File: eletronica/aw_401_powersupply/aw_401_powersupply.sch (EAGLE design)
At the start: 13 parts

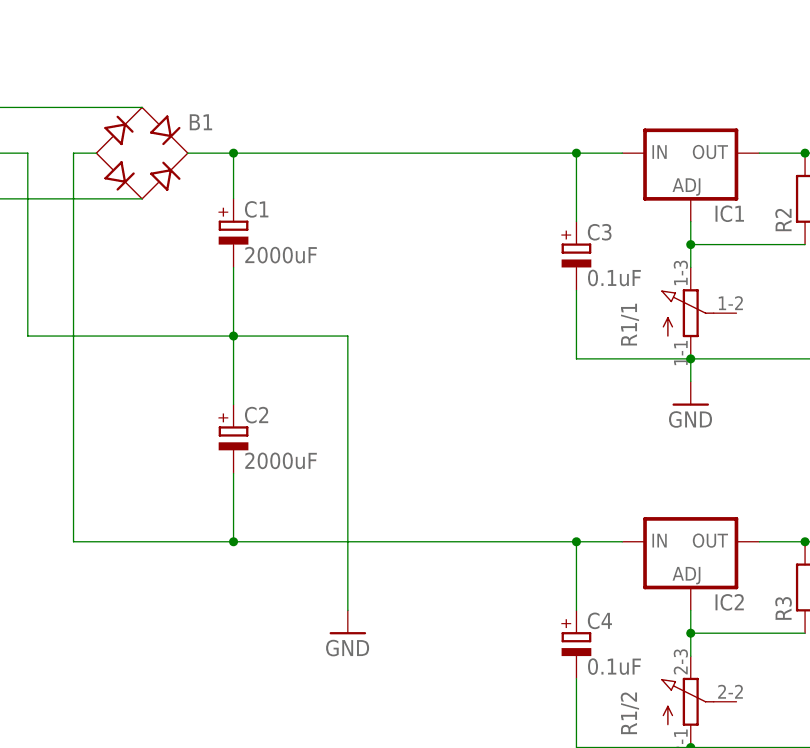
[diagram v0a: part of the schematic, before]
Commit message: 
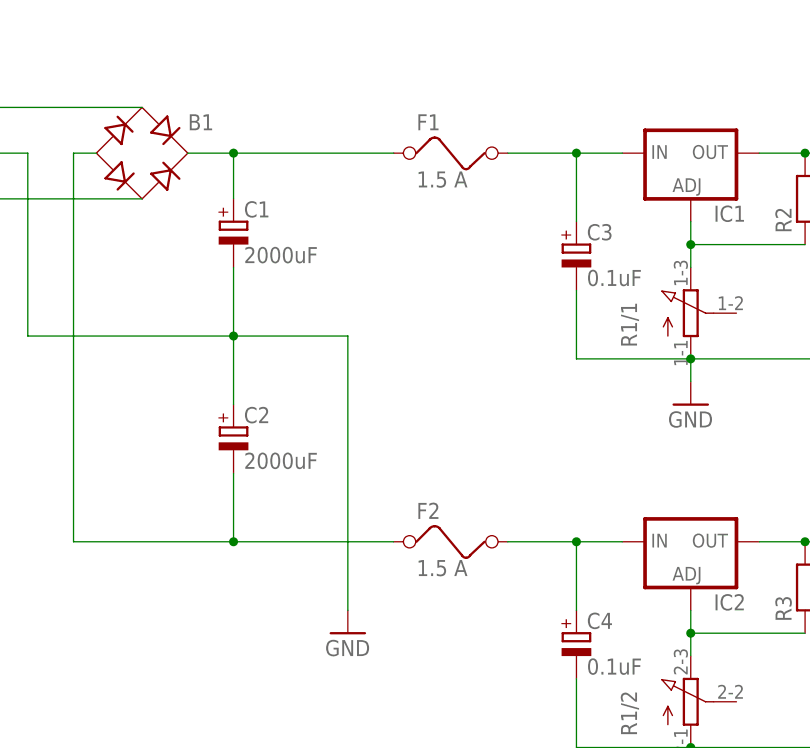
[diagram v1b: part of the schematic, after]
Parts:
- added F1, F2: 1.5 A, special:FUSE
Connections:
- new net N$10: C3.+, F1.2, IC1.IN
- new net N$9: C4.+, F2.2, IC2.IN
- net N$3: now also F1.1; no longer C3.+, IC1.IN
- net N$5: now also F2.1; no longer C4.+, IC2.IN
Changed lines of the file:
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@@
 <part name="C5" library="resistor" deviceset="CPOL-EU" device="E2.5-6" value="1uF"/>
 <part name="C6" library="resistor" deviceset="CPOL-EU" device="E2.5-6" value="1uF"/>
+<part name="F1" library="special" deviceset="FUSE" device="" value="1.5 A"/>
+<part name="F2" library="special" deviceset="FUSE" device="" value="1.5 A"/>
 </parts>
 <sheets>
@@
 <instance part="C5" gate="G$1" x="124.46" y="63.5"/>
 <instance part="C6" gate="G$1" x="124.46" y="20.32"/>
+<instance part="F1" gate="G$1" x="76.2" y="73.66"/>
+<instance part="F2" gate="G$1" x="76.2" y="30.48"/>
 </instances>
 <busses>
@@
 <wire x1="45.72" y1="73.66" x2="50.8" y2="73.66" width="0.1524" layer="91"/>
 <wire x1="50.8" y1="73.66" x2="50.8" y2="68.58" width="0.1524" layer="91"/>
-<wire x1="50.8" y1="73.66" x2="88.9" y2="73.66" width="0.1524" layer="91"/>
+<wire x1="50.8" y1="73.66" x2="68.58" y2="73.66" width="0.1524" layer="91"/>
 <junction x="50.8" y="73.66"/>
-<pinref part="IC1" gate="1" pin="IN"/>
-<pinref part="C3" gate="G$1" pin="+"/>
-<wire x1="88.9" y1="73.66" x2="93.98" y2="73.66" width="0.1524" layer="91"/>
-<wire x1="88.9" y1="73.66" x2="88.9" y2="66.04" width="0.1524" layer="91"/>
-<junction x="88.9" y="73.66"/>
+<pinref part="F1" gate="G$1" pin="1"/>
 </segment>
 </net>
@@
 <wire x1="33.02" y1="30.48" x2="50.8" y2="30.48" width="0.1524" layer="91"/>
 <wire x1="50.8" y1="30.48" x2="50.8" y2="38.1" width="0.1524" layer="91"/>
-<wire x1="50.8" y1="30.48" x2="88.9" y2="30.48" width="0.1524" layer="91"/>
+<wire x1="50.8" y1="30.48" x2="68.58" y2="30.48" width="0.1524" layer="91"/>
 <junction x="50.8" y="30.48"/>
-<pinref part="IC2" gate="1" pin="IN"/>
-<pinref part="C4" gate="G$1" pin="+"/>
-<wire x1="88.9" y1="30.48" x2="93.98" y2="30.48" width="0.1524" layer="91"/>
-<wire x1="88.9" y1="30.48" x2="88.9" y2="22.86" width="0.1524" layer="91"/>
-<junction x="88.9" y="30.48"/>
+<pinref part="F2" gate="G$1" pin="1"/>
 </segment>
 </net>
@@
 </segment>
 </net>
+<net name="N$9" class="0">
+<segment>
+<pinref part="C4" gate="G$1" pin="+"/>
+<pinref part="IC2" gate="1" pin="IN"/>
+<wire x1="88.9" y1="30.48" x2="93.98" y2="30.48" width="0.1524" layer="91"/>
+<wire x1="88.9" y1="30.48" x2="88.9" y2="22.86" width="0.1524" layer="91"/>
+<junction x="88.9" y="30.48"/>
+<wire x1="81.28" y1="30.48" x2="88.9" y2="30.48" width="0.1524" layer="91"/>
+<pinref part="F2" gate="G$1" pin="2"/>
+</segment>
+</net>
+<net name="N$10" class="0">
+<segment>
+<pinref part="C3" gate="G$1" pin="+"/>
+<pinref part="IC1" gate="1" pin="IN"/>
+<wire x1="88.9" y1="73.66" x2="93.98" y2="73.66" width="0.1524" layer="91"/>
+<wire x1="88.9" y1="73.66" x2="88.9" y2="66.04" width="0.1524" layer="91"/>
+<junction x="88.9" y="73.66"/>
+<wire x1="81.28" y1="73.66" x2="88.9" y2="73.66" width="0.1524" layer="91"/>
+<pinref part="F1" gate="G$1" pin="2"/>
+</segment>
+</net>

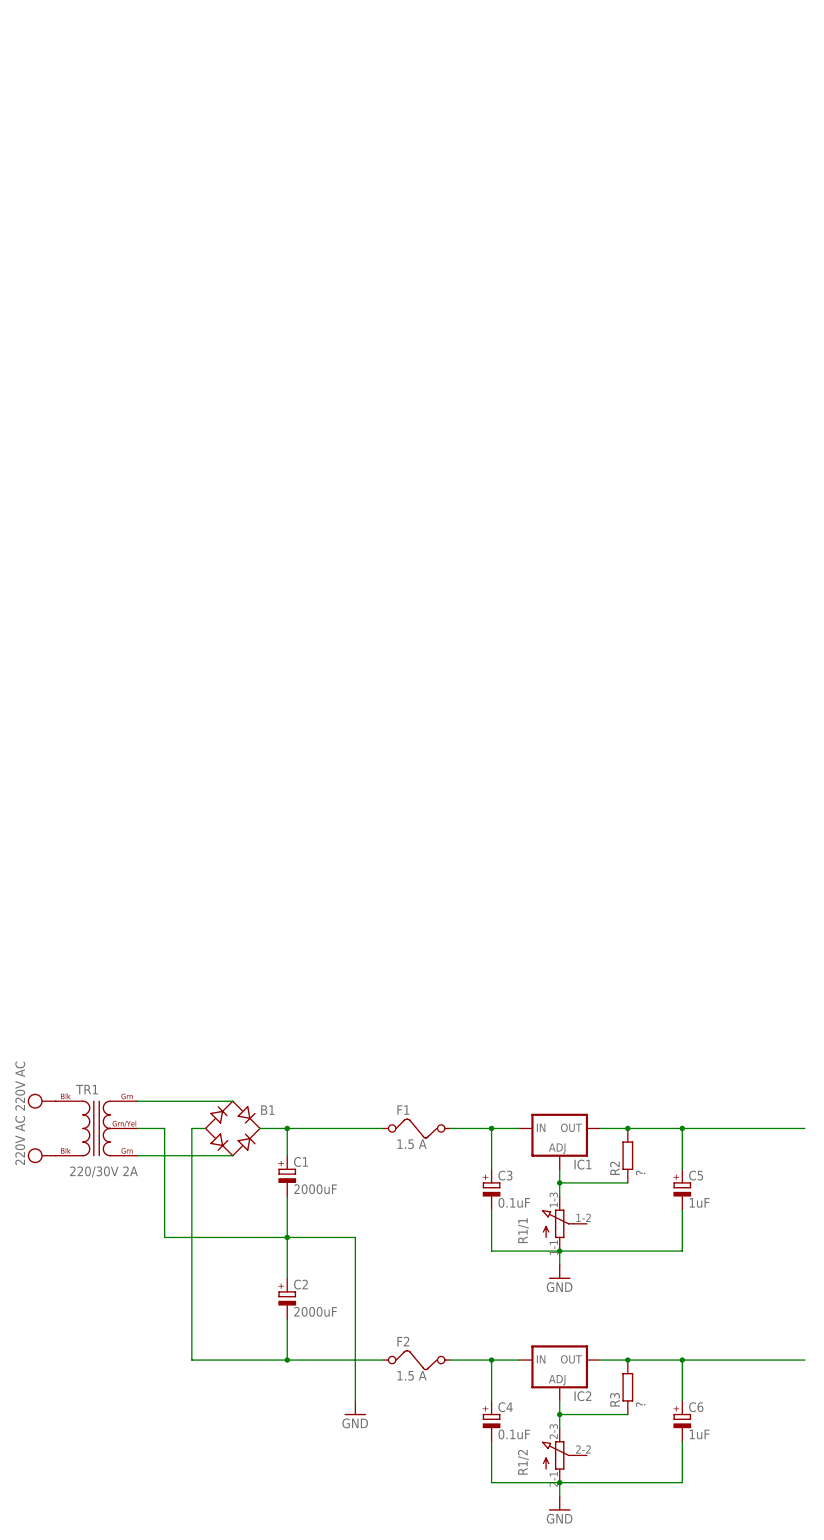
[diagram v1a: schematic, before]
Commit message: 
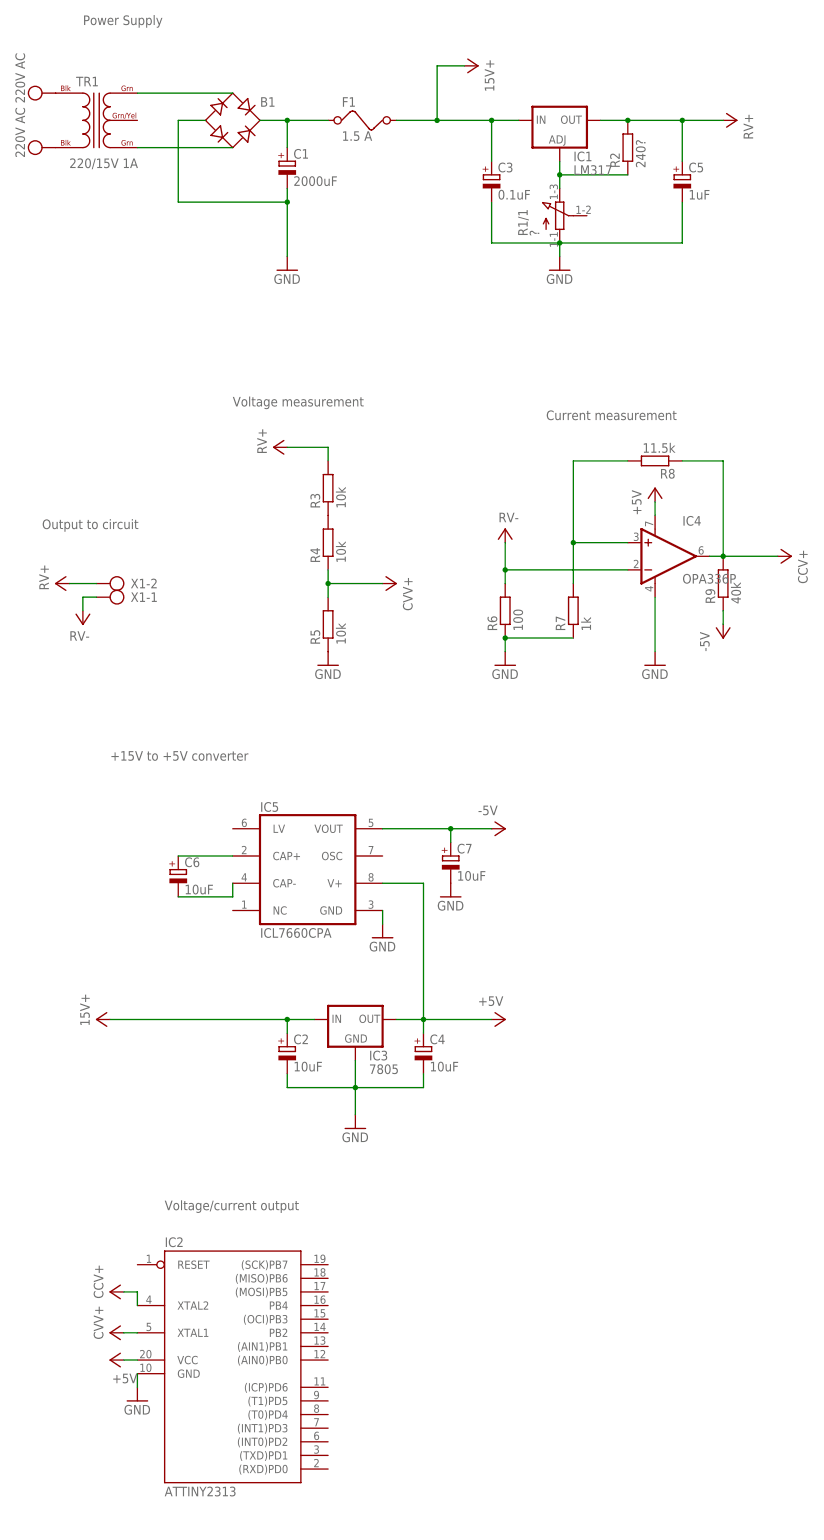
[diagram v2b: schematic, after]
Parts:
- removed F2: 1.5 A, special:FUSE
- added C7: 10uF, resistor:CPOL-EUE2.5-6
- added IC3: 7805, v-reg:78XXS
- added IC4: OPA336P, burr-brown:OPA336P
- added IC5: ICL7660CPA, maxim:ICL7660CPA
- added R4, R5: 10k, rcl:R-EU_0207/10
- added R6: 100, rcl:R-EU_0207/10
- added R7: 1k, rcl:R-EU_0207/10
- added R8: 11.5k, rcl:R-EU_0207/10
- added R9: 40k, rcl:R-EU_0207/10
- added X1: (no value), con-ptr500:AK500/2
- C2: value 2000uF -> 10uF; device resistor:CPOL-EUE3.5-8 -> resistor:CPOL-EUE2.5-6
- C4: value 0.1uF -> 10uF
- C6: value 1uF -> 10uF
- IC1: value (none) -> LM317
- IC2: value (none) -> ATTINY2313; device v-reg:LM317TS -> atmel:AT90S2313P
- R1: value (none) -> ?
- R2: value ? -> 240?
- R3: value ? -> 10k
- TR1: value 220/30V 2A -> 220/15V 1A
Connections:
- removed net N$10: C3.+, F1.2, IC1.IN
- removed net N$9: C4.+, F2.2, IC2.IN
- new net +5V: C4.+, C7.+, IC2.VCC, IC3.OUT, IC4.V+, IC5.V+, IC5.VOUT
- new net -5V: R9.1
- new net V+: C2.+, C3.+, C5.+, F1.2, IC1.IN, IC1.OUT, IC2.XTAL1, IC2.XTAL2, IC3.IN, IC4.-IN, IC4.OUT, R2.2, R3.2, R4.1, R5.2, R6.2, R8.1, R9.2, X1-1.KL, X1-2.KL
- net GND: now also B1.-, C2.-, C7.-, IC2.GND, IC3.GND, IC4.V-, IC5.GND, R5.1, R6.1, R7.1; no longer C2.+, C6.-, R1/2.A, TR1.GRN/YEL
- net N$4: now also IC5.CAP+; no longer IC2.OUT, R3.2
- net N$5: now also R3.1, R4.2; no longer B1.-, C2.-, F2.1
- net N$7: now also IC4.+IN, R7.2, R8.2; no longer IC2.ADJ, R1/2.E, R3.1
- net N$8: now also C6.-, IC5.CAP-; no longer C5.+, IC1.OUT, R2.2
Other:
- note added: "+15V to +5V converter"
- note added: "Current measurement"
- note added: "Output to circuit"
- note added: "Power Supply"
- note added: "Voltage measurement"
- note added: "Voltage/current output"
- moved on the sheet: B1, C1, C2, C3, C4, C5, C6, F1, IC1, R1/1, R2, R3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

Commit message: 
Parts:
- added DIS1, DIS2, DIS3, DIS4, DIS5, DIS6, DIS7, DIS8: HD-A101, display-hp:HD-A101
- added IC6: 4511N, 45xx:4511N
- added IC7: 74LS138N, 74xx-eu:74LS138N
- added IC8: (no value), uln-udn:ULN2803A
- added IC9: 74AC11139, 74ac-logic:74AC11139
- added R10, R11, R12, R13, R14, R15, R16, R17, R18, R19, R20, R21, R22, R23, R24, R25, R26, R27, R28, R29, R30, R31, R32: 220, rcl:R-EU_0207/10
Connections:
- new net +15V: C2.+, C3.+, F1.2, IC1.IN, IC3.IN
- new net ANODE1: DIS8.CA, DIS8.CA@1, R17.1
- new net ANODE2: DIS7.CA, DIS7.CA@1, R18.1
- new net ANODE3: DIS6.CA, DIS6.CA@1, R19.1
- new net ANODE4: DIS5.CA, DIS5.CA@1, R20.1
- new net ANODE5: DIS4.CA, DIS4.CA@1, R21.1
- new net ANODE6: DIS3.CA, DIS3.CA@1, R22.1
- new net ANODE7: DIS2.CA, DIS2.CA@1, R23.1
- new net ANODE8: DIS1.CA, DIS1.CA@1, R24.1
- new net DP1: DIS1.DP, R32.1
- new net DP2: DIS2.DP, R31.1
- new net DP3: DIS3.DP, R30.1
- new net DP4: DIS4.DP, R29.1
- new net DP5: DIS5.DP, R28.1
- new net DP6: DIS6.DP, R27.1
- new net DP7: DIS7.DP, R26.1
- new net DP8: DIS8.DP, R25.1
- new net N$10: IC2.(TXD)PD1, IC6A.IB
- new net N$11: IC2.(INT0)PD2, IC6A.IC
- new net N$12: IC2.(INT1)PD3, IC6A.ID
- new net N$13: IC6A.A, R10.2
- new net N$14: IC6A.B, R11.2
- new net N$15: IC6A.C, R12.2
- new net N$16: IC6A.D, R13.2
- new net N$17: IC6A.E, R14.2
- new net N$18: IC6A.F, R15.2
- new net N$19: IC6A.G, R16.2
- new net N$20: IC2.(ICP)PD6, IC7A.A
- new net N$21: IC2.(T1)PD5, IC7A.B
- new net N$22: IC2.(T0)PD4, IC7A.C
- new net N$23: IC7A.Y0, IC8.I1
- new net N$24: IC7A.Y1, IC8.I2
- new net N$25: IC7A.Y2, IC8.I3
- new net N$26: IC7A.Y3, IC8.I4
- new net N$27: IC9B.Y0, R25.2
- new net N$28: IC9A.Y3, R32.2
- new net N$29: IC9A.Y2, R31.2
- new net N$30: IC9A.Y1, R30.2
- new net N$31: IC9A.Y0, R29.2
- new net N$32: IC9B.Y3, R28.2
- new net N$33: IC9B.Y2, R27.2
- new net N$34: IC7A.Y4, IC8.I5
- new net N$35: IC7A.Y5, IC8.I6
- new net N$36: IC7A.Y6, IC8.I7
- new net N$37: IC7A.Y7, IC8.I8
- new net N$38: IC9B.Y1, R26.2
- new net N$46: IC8.O1, R17.2
- new net N$47: IC8.O2, R18.2
- new net N$48: IC8.O3, R19.2
- new net N$49: IC8.O4, R20.2
- new net N$50: IC8.O5, R21.2
- new net N$51: IC8.O6, R22.2
- new net N$52: IC8.O7, R23.2
- new net N$53: IC8.O8, R24.2
- new net N$54: IC2.(AIN0)PB0, IC9A.B
- new net N$55: IC2.(AIN1)PB1, IC9A.A
- new net N$56: IC2.PB2, IC9B.B
- new net N$57: IC2.(OCI)PB3, IC9B.A
- new net N$9: IC2.(RXD)PD0, IC6A.IA
- new net PORT0: DIS1.A, R10.1
- new net PORT1: DIS1.B, R11.1
- new net PORT2: DIS1.C, R12.1
- new net PORT3: DIS1.D, R13.1
- new net PORT4: DIS1.E, R14.1
- new net PORT5: DIS1.F, R15.1
- new net PORT6: DIS1.G, R16.1
- new net VCCIO: IC2.XTAL1, IC2.XTAL2, IC4.OUT, R4.1, R5.2, R8.1, R9.2
- net +5V: now also IC6A.BI, IC6A.LT, IC7A.G1, IC8.CD+, IC9A.G, IC9B.G; no longer C7.+, IC5.VOUT
- net -5V: now also C7.+, IC5.VOUT
- net GND: now also IC6A.LE, IC7A.G2A, IC7A.G2B, IC8.GND
- net V+: no longer C2.+, C3.+, F1.2, IC1.IN, IC2.XTAL1, IC2.XTAL2, IC3.IN, IC4.OUT, R4.1, R5.2, R8.1, R9.2
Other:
- moved on the sheet: B1, C1, C2, C3, C4, C5, C6, C7, F1, IC1, IC2, IC3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

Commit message: 
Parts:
- removed F1: 1.5 A, special:FUSE
- removed X1: (no value), con-ptr500:AK500/2
- added D1: (no value), diode:ZENER-DIODEC1702-15
- added F2: 1.5 A, special:FUSE
- added R33: 10k, rcl:R-EU_0207/10
- added S1: (no value), switch:255SB
- added T1: 2N1613, transistor:2N1613
- added X2: (no value), con-ptr500:AK500/2
- IC8: value (none) -> ULN2803
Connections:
- new net N$39: S1.S, TR1.BLK@1
- new net N$40: F2.2, S1.P
- net +15V: now also B1.+, C1.+; no longer F1.2
- net GND: now also TR1.GRN/YEL
- net N$3: now also D1.A, R33.2, T1.B; no longer B1.+, C1.+, F1.1
- net V+: now also D1.C, R33.1, T1.C, T1.E, X2-1.KL, X2-2.KL; no longer X1-1.KL, X1-2.KL
- net VDD: now also F2.1; no longer TR1.BLK@1
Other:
- note added: "Crowbar and output to circuit"
- note removed: "Output to circuit"
- moved on the sheet: B1, C1, C3, C5, IC1, IC4, R1/1, R2, R3, R4, R5, R6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
